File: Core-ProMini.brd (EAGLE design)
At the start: 99.8 x 80.5 mm, 94 parts, among them J1 RJ12, J3 CONNECTOR-GROVE-4P-2.0-347013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, J4 CONNECTOR-DC-POWER-RA, J8 RJ12, Q1 2N3904, Q10 MOSFET-P-044021001, Q11 MOSFET-P-044021001, Q12 MOSFET-P-044021001, Q13 MOSFET-P-044021001, Q4 MOSFET-P mouser 78-SI2347DS-T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, Q5 MOSFET-P-044021001, Q6 MOSFET-P-044021001, Q7 MOSFET-P-044021001, Q8 MOSFET-P-044021001, Q9 MOSFET-P-044021001, U1 LM393M, U2 LM317

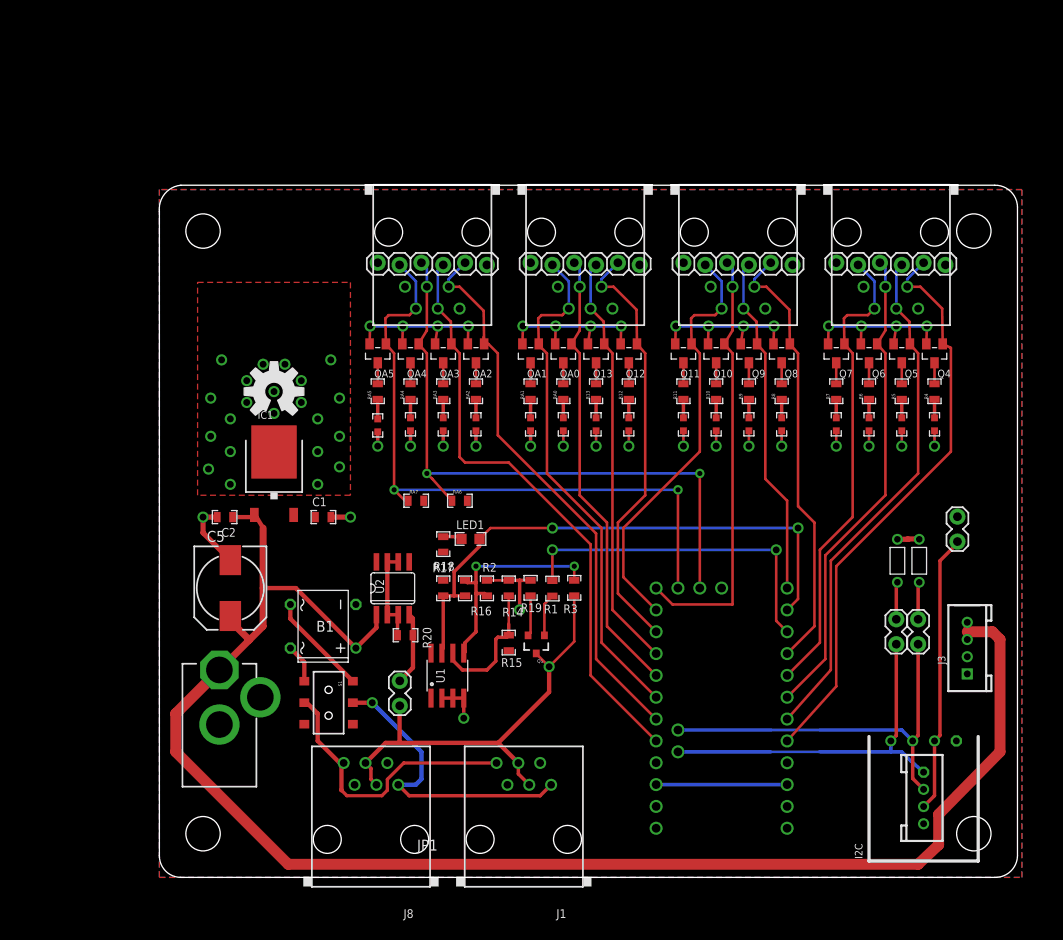
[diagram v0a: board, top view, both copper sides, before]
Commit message: removed loconet interface
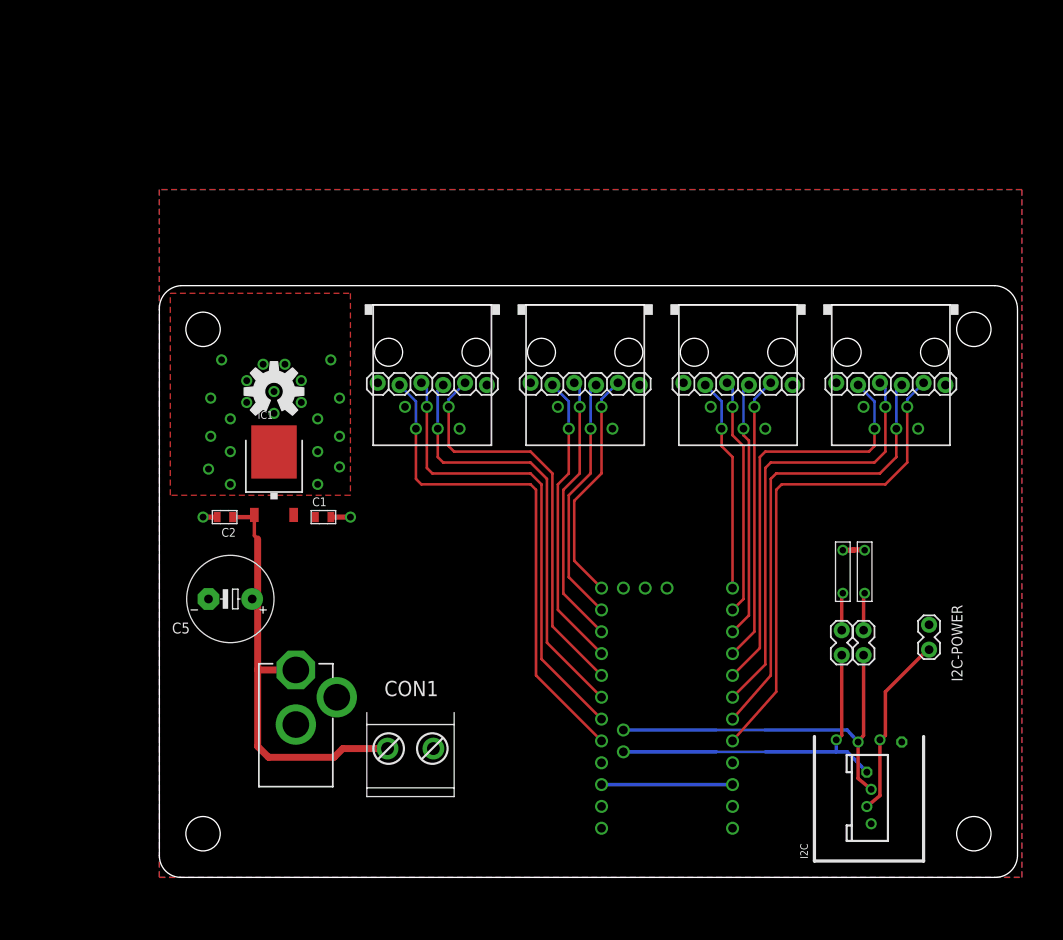
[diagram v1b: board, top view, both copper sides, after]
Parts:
- removed B1: DBDB101G, rectifier:DB
- removed J1, J8: RJ12, SPCoast:RJ25
- removed J3: CONNECTOR-GROVE-4P-2.0-3470130P1, SPCoast:4P-2.0
- removed JP1: LN-TERM, MCP:1X02_LOCK
- removed JP5: I2C Power, SparkFun-Connectors:1X02_LOCK
- removed LED1: Blue, SPCoast:0805-LED
- removed LED10, LED11, LED12, LED13, LED4, LED5, LED6, LED7, LED8, LED9, LEDA0, LEDA1, LEDA2, LEDA3, LEDA4, LEDA5: Y-0330050P1, SPCoast:0603-LED
- removed Q1: 2N3904, MCP:SOT23-3
- removed Q10, Q11, Q12, Q13, Q5, Q6, Q7, Q8, Q9, QA0, QA1, QA2, QA3, QA4, QA5: MOSFET-P-044021001, SPCoast:SOT23
- removed Q4: MOSFET-P mouser 78-SI2347DS-T1-GE3 30V .042Ohm@10V 5A P-Ch 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, SPCoast:SOT23
- removed R1: 4k7, SPCoast:0805-RES
- removed R10, R11, R12, R13, R4, R5, R6, R7, R8, R9, RA0, RA1, RA2, RA3, RA4, RA5: 2K2, SPCoast:0805-RES
- removed R14: 39k, SPCoast:0805-RES
- removed R15: 27k, SPCoast:0805-RES
- removed R16: 240k, SPCoast:0805-RES
- removed R17: 1k, SPCoast:0805-RES
- removed R18: 470R, SPCoast:0805-RES
- removed R19: 47R, SPCoast:0805-RES
- removed R2: 150k, SPCoast:0805-RES
- removed R20: 82R, SPCoast:0805-RES
- removed R3: 47k, SPCoast:0805-RES
- removed RA6, RA7: 10k, SPCoast:0805-RES
- removed S1: DPDT, SPCoast:AYZ0202
- removed U1: LM393M, MCP:SO08@1
- removed U2: LM317, MCP:SO08
- added CON1: (no value), SPCoast:MSTB2
- added I2C-POWER: (no value), SPCoast:1X02_LOCK
- C5: device SPCoast:0810-CAP -> SPCoast:E5-10.5
- J4: value CONNECTOR-DC-POWER-RA -> (none)
- JP10, JP11, JP12, JP13: device SparkFun-Connectors:1X06_LOCK -> SPCoast:1X06_LOCK
- R111: value 1k8 -> 2k-5k
- U$4: value BOARD80X100 -> BOARD69X100MRCS; device SPCoast:BOARD-DINRAIL-3.17IN -> SPCoast:BOARD-DINRAIL-2.71IN-MRCS
- moved LOGO1 69.9 mm to (5.08, 5.08)
- moved J2 14.0 mm to (85.1, 61.1)
- moved J5 14.0 mm to (67.3, 61.1)
- moved J6 14.0 mm to (49.5, 61.1)
- moved J7 14.0 mm to (31.8, 61.1)
- moved JP10 14.0 mm to (91.4, 57.3)
- moved JP11 14.0 mm to (73.7, 57.3)
- moved JP12 14.0 mm to (55.9, 57.3)
- moved JP13 14.0 mm to (38.1, 57.3)
- moved U$3 10.2 mm to (23.1, 8.13)
- moved J4 8.89 mm to (15.9, 21.0)
- moved R111 6.48 mm to (79.5, 35.6)
- moved JP2 6.48 mm to (81.9, 28.6)
- moved JP3 6.48 mm to (79.4, 28.6)
- moved R101 6.48 mm to (82.0, 35.6)
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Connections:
- removed net LNRX: LED1.C, R16.2, R17.2, U$2.D8, U1.7
- removed net LNTX: R1.1, U$2.D7
- removed net LOCONET: J1.3, J1.4, J8.3, J8.4, JP1.1, Q1.3, R3.1
- removed net N$1: Q1.1, R1.2
- removed net N$10: LED6.A, R6.1
- removed net N$11: Q1.2, R19.1
- removed net N$12: Q5.3, R5.2
- removed net N$13: Q6.3, R6.2
- removed net N$14: Q7.3, R7.2
- removed net N$15: LED7.A, R7.1
- removed net N$16: LED11.A, R11.1
- removed net N$17: LED10.A, R10.1
- removed net N$18: LED9.A, R9.1
- removed net N$19: Q8.3, R8.2
- removed net N$20: Q9.3, R9.2
- removed net N$21: Q10.3, R10.2
- removed net N$22: Q11.3, R11.2
- removed net N$23: LED8.A, R8.1
- removed net N$24: LED12.A, R12.1
- removed net N$25: LED13.A, R13.1
- removed net N$26: LEDA0.A, RA0.1
- removed net N$27: Q12.3, R12.2
- removed net N$28: LEDA1.A, RA1.1
- removed net N$29: Q13.3, R13.2
- removed net N$30: JP1.2, R20.2, U2.4
- removed net N$31: B1.AC1, S1.1
- removed net N$32: B1.AC2, S1.4
- removed net N$33: QA0.3, RA0.2
- removed net N$34: QA1.3, RA1.2
- removed net N$35: LEDA5.A, RA5.1
- removed net N$36: LEDA4.A, RA4.1
- removed net N$37: LEDA3.A, RA3.1
- removed net N$38: LEDA2.A, RA2.1
- removed net N$39: QA2.3, RA2.2
- removed net N$4: R16.1, R2.2, R3.2, U1.5
- removed net N$40: QA3.3, RA3.2
- removed net N$41: QA4.3, RA4.2
- removed net N$42: QA5.3, RA5.2
- removed net N$5: R14.2, R15.2, U1.6
- removed net N$6: LED1.A, R18.2
- removed net N$7: LED4.A, R4.1
- removed net N$8: Q4.3, R4.2
- removed net N$9: LED5.A, R5.1
- removed net RAILSYNC-A: J1.6, J8.6, S1.2
- removed net RAILSYNC-B: J1.1, J8.1, S1.5
- removed net VOUT: R20.1, U2.2, U2.3, U2.6, U2.7
- new net D7: J5.3, JP11.3, U$2.D7
- new net D8: J5.4, JP11.4, U$2.D8
- net +9V: now also CON1.1; no longer B1.+, J3.3, J3.4, U2.1
- net A0: now also J7.2, JP13.2; no longer J6.4, JP12.4, QA0.1
- net A1: now also J7.3, JP13.3; no longer J6.5, JP12.5, QA1.1
- net A2: now also J7.4, JP13.4; no longer J7.2, JP13.2, QA2.1
- net A3: now also J7.5, JP13.5; no longer J7.3, JP13.3, QA3.1
- net A6: no longer J7.4, JP13.4, QA4.1, RA6.1
- net A7: no longer J7.5, JP13.5, QA5.1, RA7.1
- net D10: now also J6.2, JP12.2; no longer J5.4, JP11.4, Q10.1
- net D11: now also J6.3, JP12.3; no longer J5.5, JP11.5, Q11.1
- net D12: now also J6.4, JP12.4; no longer J6.2, JP12.2, Q12.1
- net D13: now also J6.5, JP12.5; no longer J6.3, JP12.3, Q13.1
- net D2: no longer Q4.1
- net D3: no longer Q5.1
- net D4: no longer Q6.1
- net D5: no longer Q7.1
- net D6: no longer Q8.1
- net D9: now also J5.5, JP11.5; no longer J5.3, JP11.3, Q9.1
- net GND: now also CON1.2; no longer B1.-, J1.2, J1.5, J3.1, J3.2, J8.2, J8.5, LED10.C, LED11.C, LED12.C, LED13.C, LED4.C, LED5.C, LED6.C, LED7.C, LED8.C, LED9.C, LEDA0.C, LEDA1.C, LEDA2.C, LEDA3.C, LEDA4.C, LEDA5.C, R14.1, R19.2, R2.1, U1.2, U1.3, U1.4
- net N$44: now also I2C-POWER.1; no longer JP5.1
- net VCCIO: now also I2C-POWER.2; no longer JP5.2, Q10.2, Q11.2, Q12.2, Q13.2, Q4.2, Q5.2, Q6.2, Q7.2, Q8.2, Q9.2, QA0.2, QA1.2, QA2.2, QA3.2, QA4.2, QA5.2, R15.1, R17.1, R18.1, RA6.2, RA7.2, U1.8
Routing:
- net +9V: track 185.2 -> 51.1 mm
- net VCCIO: track 83.1 -> 4.03 mm, vias 16 -> 0
- net A7: track 76.8 -> 0.00 mm, vias 2 -> 0
- net A6: track 74.8 -> 0.00 mm, vias 2 -> 0
- net LNRX: track 64.8 -> 0.00 mm, vias 2 -> 0
- net LOCONET: track 53.1 -> 0.00 mm, vias 1 -> 0
- net GND: track 52.1 -> 3.92 mm, vias 42 -> 24
- net LNTX: track 39.7 -> 0.00 mm, vias 2 -> 0
- net RAILSYNC-A: track 35.3 -> 0.00 mm, vias 1 -> 0
- net RAILSYNC-B: track 33.3 -> 0.00 mm
- net D7: track 0.00 -> 30.0 mm
- net D8: track 0.00 -> 27.7 mm
- net N$4: track 26.5 -> 0.00 mm, vias 2 -> 0
- net D10: track 50.3 -> 27.3 mm
- net D11: track 49.4 -> 29.1 mm
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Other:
- board size 99.8 x 80.5 mm -> 99.8 x 68.8 mm
- board text added: "+ --"
- board text added: "1.0A"
- board text added: "2k-5k"
- board text added: "3.0 2017.05"
- board text added: "Core-ProMini"
- board text added: "D7"
- board text added: "D8"
- board text removed: "(input only)"
- board text removed: "*"
- board text removed: "+ -"
- board text removed: "1.5A"
- board text removed: "1k8"
- board text removed: "2.0A 2015.01"
- board text removed: "2015.01"
- board text removed: "=LNRX"
- board text removed: "=LNTX"
- board text removed: "A6"
- board text removed: "A7"
- board text removed: "Activity"
- board text removed: "LNet TERM"
- board text removed: "Note: D8/D7 reserved for LNet Rx/Tx"
- board text removed: "RailSync Brd Power"
- board text removed: "To Lnet"
- board text removed: "UNO"
- board text removed: "off"
- board text removed: "on"
- board text removed: "v2.0A"

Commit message: updated part values and silkscreen, added cmri-io
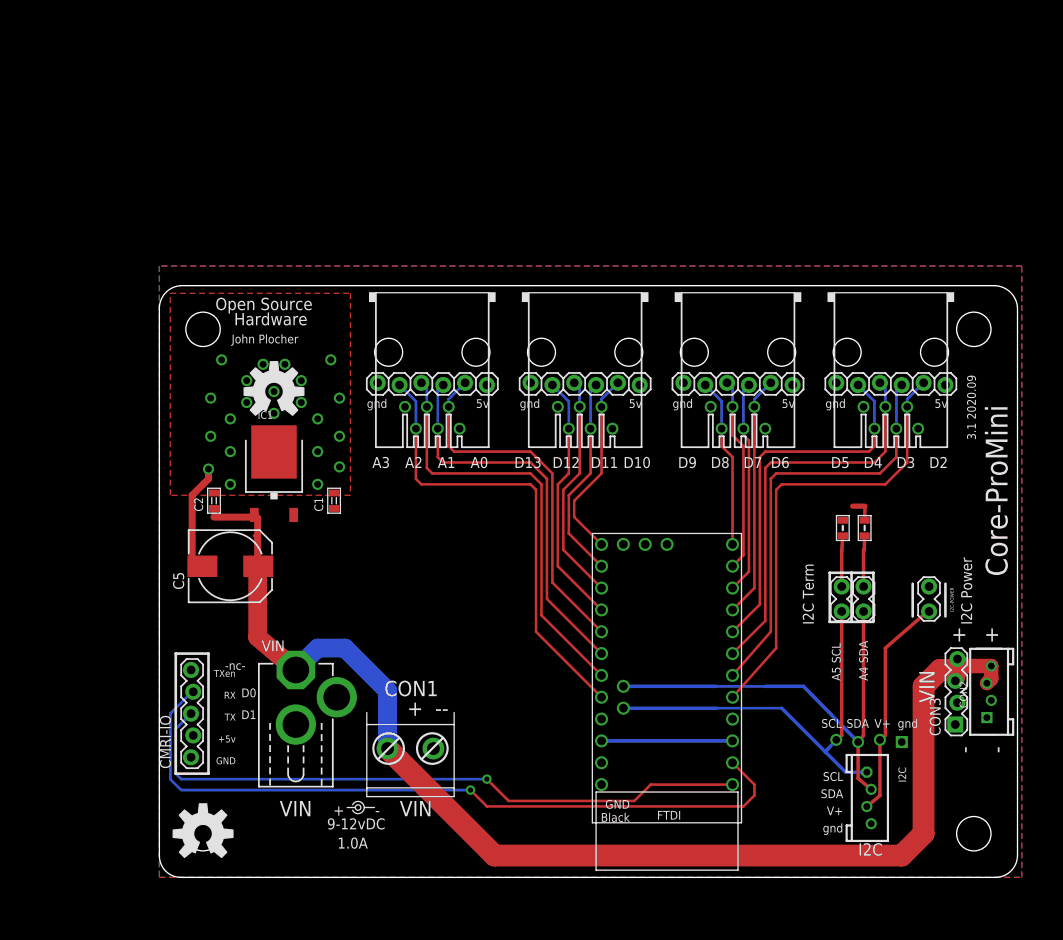
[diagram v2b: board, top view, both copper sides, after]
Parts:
- removed JP2: SDA, SPCoast:1X02_LOCK
- removed JP3: SCL, SPCoast:1X02_LOCK
- added CMRI-IO: 0.100, SPCoast:1X05-CMRI-IO
- added CON2: 2mm, SPCoast:4P-2.0
- added CON3: 0.100, SPCoast:1X04_LOCK
- added SCL, SDA: 0.100, SPCoast:1X02_LOCK
- C5: device SPCoast:E5-10.5 -> SPCoast:0810-CAP
- CON1: value (none) -> 5.08
- I2C: value CONNECTOR-I2CLEFT -> I2C
- I2C-POWER, JP10, JP11, JP12, JP13: value (none) -> 0.100
- IC1: value (none) -> cj7805; device SPCoast:TO252 -> SPCoast:TO-252
- J2, J5, J6, J7: value (none) -> IO4; device SPCoast:RJ11-NO_SHIELD -> SPCoast:RJ25-PANEL
- J4: value (none) -> 2.1mm
- LOGO1: value DOC-OSHW-LOGOL -> DOC-OSHW-LOGO-L
- R101, R111: device SPCoast:1/6W-RES -> SPCoast:0805-RES
- U$3: device SPCoast-minimal:POWER_USAGE -> SPCoast:PWR_LABEL
- moved U$2 5.08 mm to (67.9, 40.0)
- moved R101 5.08 mm to (82.0, 40.6)
- moved R111 5.08 mm to (79.5, 40.6)
- moved I2C-POWER 4.44 mm to (89.5, 31.1)
- moved C5 3.81 mm to (8.26, 36.2), turned to 0 degrees
- moved C1 2.29 mm to (20.3, 43.8), turned to 90 degrees
- moved C2 2.29 mm to (6.35, 43.8), turned to 90 degrees
- turned IC1 to 90 degrees
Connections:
- net +9V: now also CON2.3, CON2.4, CON3.3, CON3.4
- net D0: now also CMRI-IO.4
- net D1: now also CMRI-IO.3
- net GND: now also CMRI-IO.1, CON2.1, CON2.2, CON3.1, CON3.2
- net N$2: now also SCL.1; no longer JP3.1
- net N$3: now also SDA.1; no longer JP2.1
- net SCL: now also SCL.2; no longer JP3.2
- net SDA: now also SDA.2; no longer JP2.2
- net VCCIO: now also CMRI-IO.2
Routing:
- net +9V: track 51.1 -> 148.0 mm
- net D0: track 0.00 -> 86.0 mm, vias 0 -> 1
- net D1: track 0.00 -> 74.6 mm, vias 0 -> 1
- net GND: track 3.92 -> 13.4 mm, vias 24 -> 22
- net SCL: track 40.9 -> 48.5 mm
- net SDA: track 44.5 -> 51.7 mm
- net D5: track 48.5 -> 43.4 mm
- net D4: track 51.3 -> 46.2 mm
- net D11: track 29.1 -> 24.0 mm
- net A2: track 54.5 -> 49.4 mm
- net D8: track 27.7 -> 22.7 mm
- net D9: track 24.9 -> 19.9 mm
- net D7: track 30.0 -> 24.9 mm
- net D6: track 33.3 -> 28.3 mm
- net D3: track 53.9 -> 48.8 mm
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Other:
- board text added: "+"
- board text added: "-"
- board text added: "-nc-"
- board text added: "1k8"
- board text added: "3.1 2020.09"
- board text added: "5v"
- board text added: "A4 SDA"
- board text added: "A5 SCL"
- board text added: "D0"
- board text added: "D1"
- board text added: "I2C Power"
- board text added: "gnd"
- board text removed: "2k-5k"
- board text removed: "3.0 2017.05"
- board text removed: "A4"
- board text removed: "A5"

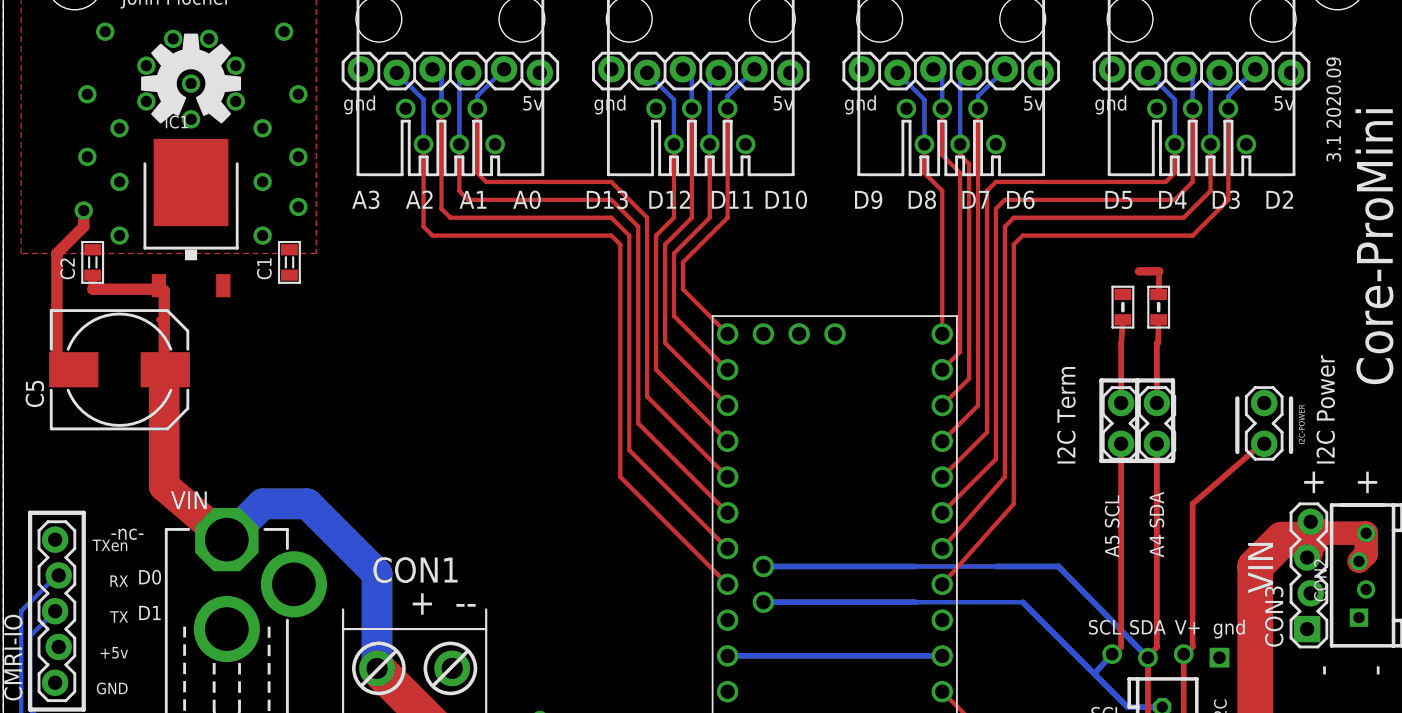
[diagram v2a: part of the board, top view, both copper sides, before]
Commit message: updated part names
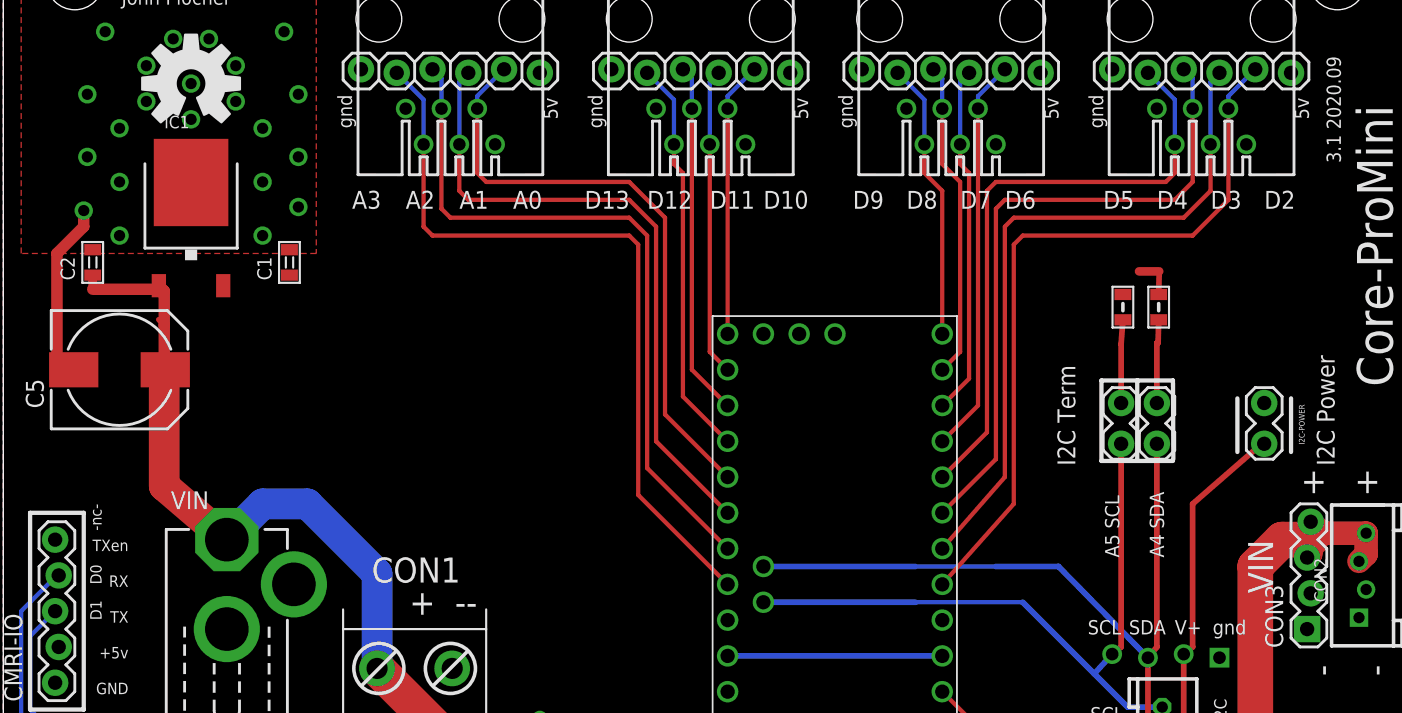
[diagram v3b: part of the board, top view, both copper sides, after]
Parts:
- OSH: value DOC-OSHW-LOGO-L -> L
- renumbered LOGO1 to OSH, U$2 to CPU, U$3 to PWR, U$4 to BOARD
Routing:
- net D10: track 22.2 -> 19.6 mm
- net D11: track 24.0 -> 21.9 mm
- net D12: track 26.8 -> 25.2 mm
- net D13: track 29.6 -> 28.5 mm
- net A2: track 49.4 -> 50.2 mm
- net A0: track 42.3 -> 43.1 mm
- net A3: track 53.5 -> 54.2 mm
- net A1: track 45.3 -> 46.1 mm

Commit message: updated part names
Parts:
- removed U$1: OSHW-LOGOL, SparkFun:OSHW-LOGO-L
- OSH: device SPCoast:OSHW-LOGO-L -> SparkFun:OSHW-LOGO-L
- moved OSH 52.1 mm to (13.3, 56.5)
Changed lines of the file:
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@@
 <attribute name="VALUE" x="77.6732" y="30.6832" size="1.016" layer="27" ratio="10" rot="SR90"/>
 </element>
-<element name="U$1" library="SparkFun" package="OSHW-LOGO-L" value="OSHW-LOGOL" x="13.335" y="56.515"/>
+<element name="OSH" library="SparkFun" package="OSHW-LOGO-L" value="L" x="13.335" y="56.515"/>
 <element name="J2" library="SPCoast" package="RJ25-PANEL" value="IO4" x="85.09" y="61.087" smashed="yes" rot="R180">
 <attribute name="VALUE" x="90.805" y="58.547" size="1.778" layer="27" rot="R180"/>
@@
 <element name="C1" library="SPCoast" package="0805-CAP" value="1uF" x="20.32" y="43.815" rot="R90"/>
 <element name="C2" library="SPCoast" package="0805-CAP" value="1uF" x="6.35" y="43.815" rot="R90"/>
-<element name="OSH" library="SPCoast" package="OSHW-LOGO-L" value="L" x="5.08" y="5.08"/>
 <element name="IC1" library="SPCoast" package="TO-252" value="cj7805" x="13.335" y="46.99" rot="R90"/>
 <element name="CON1" library="SPCoast" package="MSTB2" value="5.08" x="29.21" y="13.97" smashed="yes">
